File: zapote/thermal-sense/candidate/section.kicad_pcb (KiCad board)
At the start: 2 copper layers, 66 x 43 mm, 17 parts, among them J1 B2B-XH-A(LF)(SN), J2 B2B-XH-A(LF)(SN), J3 B6B-XH-A(LF)(SN), U1 TLV3201AIDBVR, U2 TLV3201AIDBVR

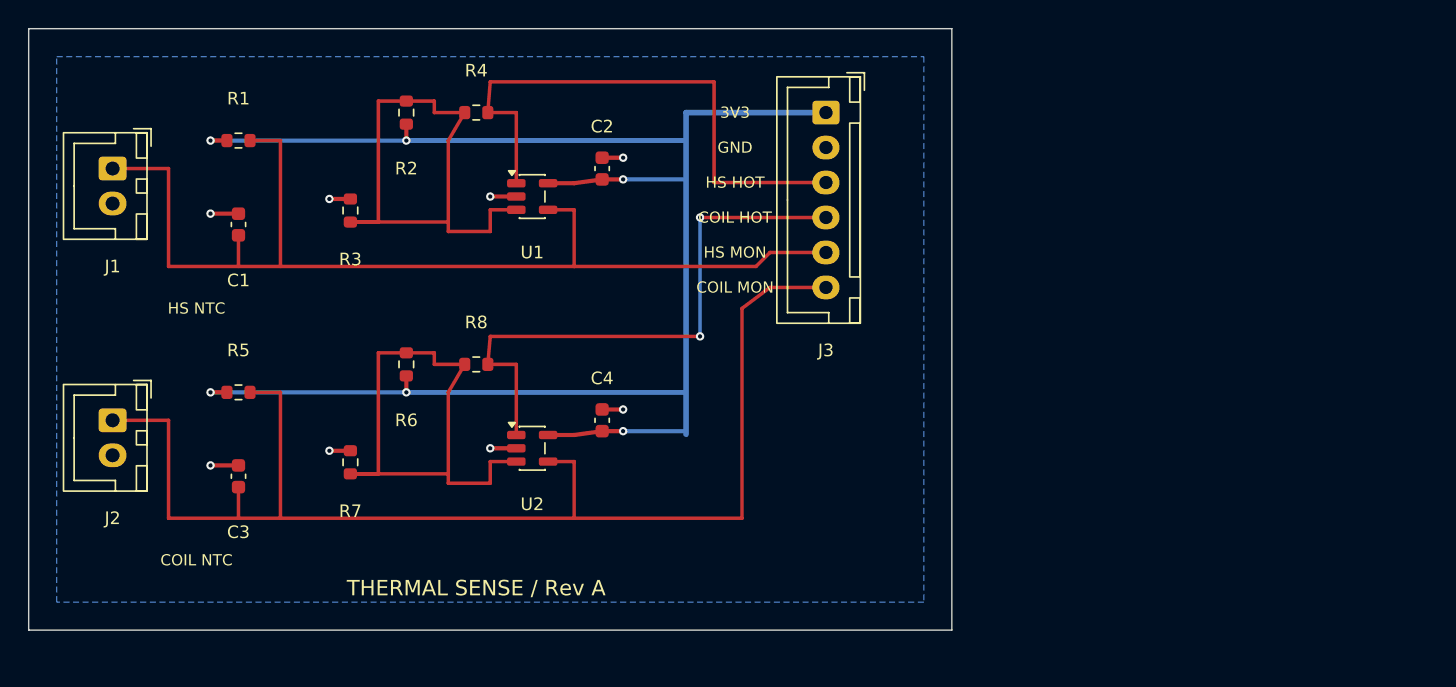
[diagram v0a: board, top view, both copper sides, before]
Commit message: fix(zapote): detect disconnected thermal sensors in hardware
Add per-channel open comparators and OR gates, retune the coil network,
and route Rev B. Bind Rust fault-margin and threshold-crossing checks to
the source, with real Rev A and capacitor counterexamples. Preserve
qualification limits, native evidence and versioned memory notes.
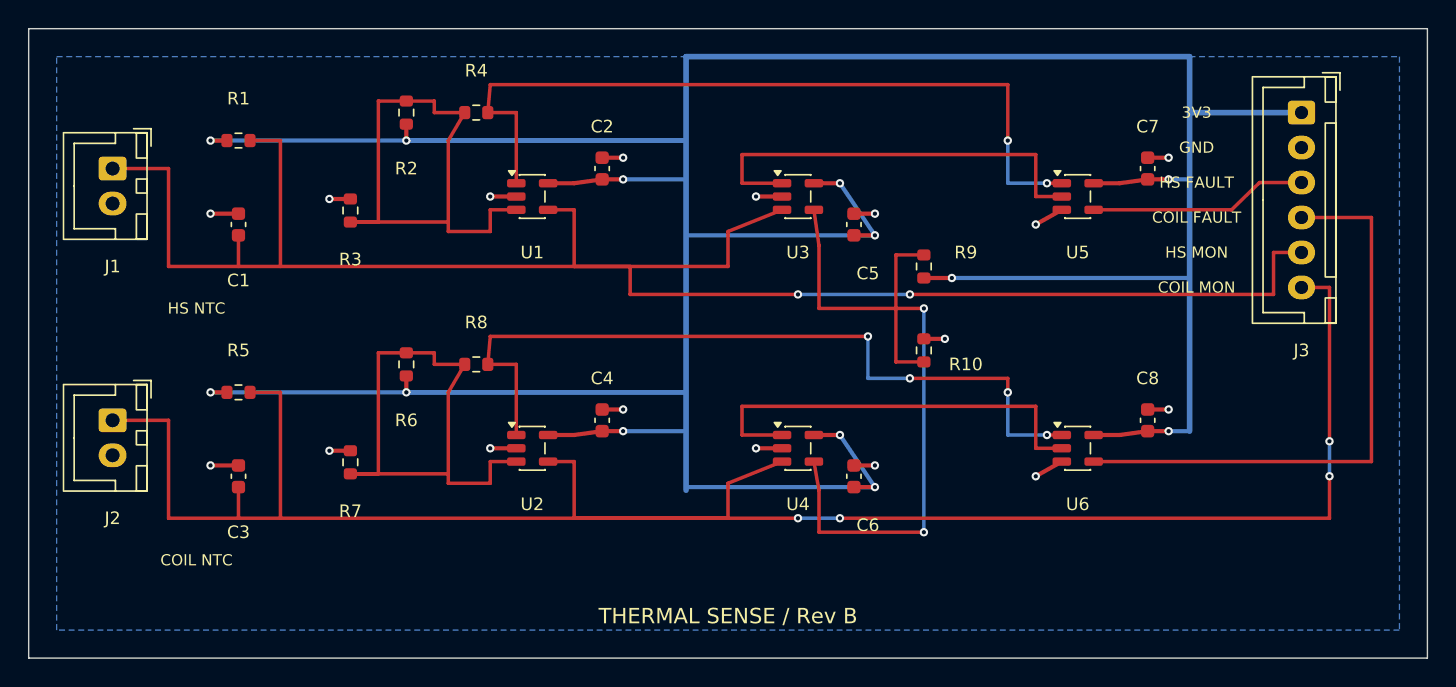
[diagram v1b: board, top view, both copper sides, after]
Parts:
- added C5: C0603C104K5RACTU, Capacitor_SMD:C_0603_1608Metric, F.Cu at (59.0, 14.0)
- added C6: C0603C104K5RACTU, Capacitor_SMD:C_0603_1608Metric, F.Cu at (59.0, 32.0)
- added C7: C0603C104K5RACTU, Capacitor_SMD:C_0603_1608Metric, F.Cu at (80.0, 10.0)
- added C8: C0603C104K5RACTU, Capacitor_SMD:C_0603_1608Metric, F.Cu at (80.0, 28.0)
- added R10: RC0603FR-07100KL, Resistor_SMD:R_0603_1608Metric, F.Cu at (64.0, 23.0)
- added R9: RC0603FR-071K21L, Resistor_SMD:R_0603_1608Metric, F.Cu at (64.0, 17.0)
- added U3: TLV9031DBVR, Package_TO_SOT_SMD:SOT-23-5, F.Cu at (55.0, 12.0)
- added U4: TLV9031DBVR, Package_TO_SOT_SMD:SOT-23-5, F.Cu at (55.0, 30.0)
- added U5: SN74LVC1G32DBVR, Package_TO_SOT_SMD:SOT-23-5, F.Cu at (75.0, 12.0)
- added U6: SN74LVC1G32DBVR, Package_TO_SOT_SMD:SOT-23-5, F.Cu at (75.0, 30.0)
- R5: value RC0603FR-073K32L -> RC0603FR-0710KL
- R6: value RC0603FR-073K16L -> RC0603FR-0720KL
- R7: value RC0603FR-074K42L -> RC0603FR-078K06L
- R8: value RC0603FR-0711K5L -> RC0603FR-0742K2L
- moved J3 34.0 mm to (91.0, 6.00)
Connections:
- R4 pad 2: HS_FAULT -> HS_HOT
- R8 pad 2: COIL_FAULT -> COIL_HOT
- U1 pad 1: HS_FAULT -> HS_HOT
- U2 pad 1: COIL_FAULT -> COIL_HOT
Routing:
- net +3V3: track 165.5 -> 309.7 mm, vias 6 -> 13
- net HS_HOT: track 0.00 -> 57.0 mm, vias 0 -> 2
- net COIL_HOT: track 0.00 -> 57.0 mm, vias 0 -> 4
- net COIL_SENSE: track 92.8 -> 149.5 mm, vias 0 -> 4
- net HS_SENSE: track 77.7 -> 134.0 mm, vias 0 -> 2
- net OPEN_REF: track 0.00 -> 54.8 mm, vias 0 -> 2
- net HS_OPEN: track 0.00 -> 30.8 mm
- net COIL_OPEN: track 0.00 -> 30.8 mm
- net HS_FAULT: track 40.5 -> 15.7 mm
- net gnd: track 13.7 -> 29.2 mm, vias 8 -> 17
- net COIL_FAULT: track 41.6 -> 42.3 mm, vias 2 -> 0
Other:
- board size 66 x 43 mm -> 100 x 45 mm
- board text added: "COIL FAULT"
- board text added: "HS FAULT"
- board text added: "THERMAL SENSE / Rev B"
- board text removed: "COIL HOT"
- board text removed: "HS HOT"
- board text removed: "THERMAL SENSE / Rev A"
